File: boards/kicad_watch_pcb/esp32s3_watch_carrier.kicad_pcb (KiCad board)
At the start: 2 copper layers, 180 x 120 mm, 15 parts, among them J1 ESP32-S3 GPIO BUS, J2 ST7735 128x128, J3 I2S MIC, J4 MAX98357A, J5 MPU6050, J6 POWER, SW1 P4, SW2 P5, SW3 P6, SW4 P7

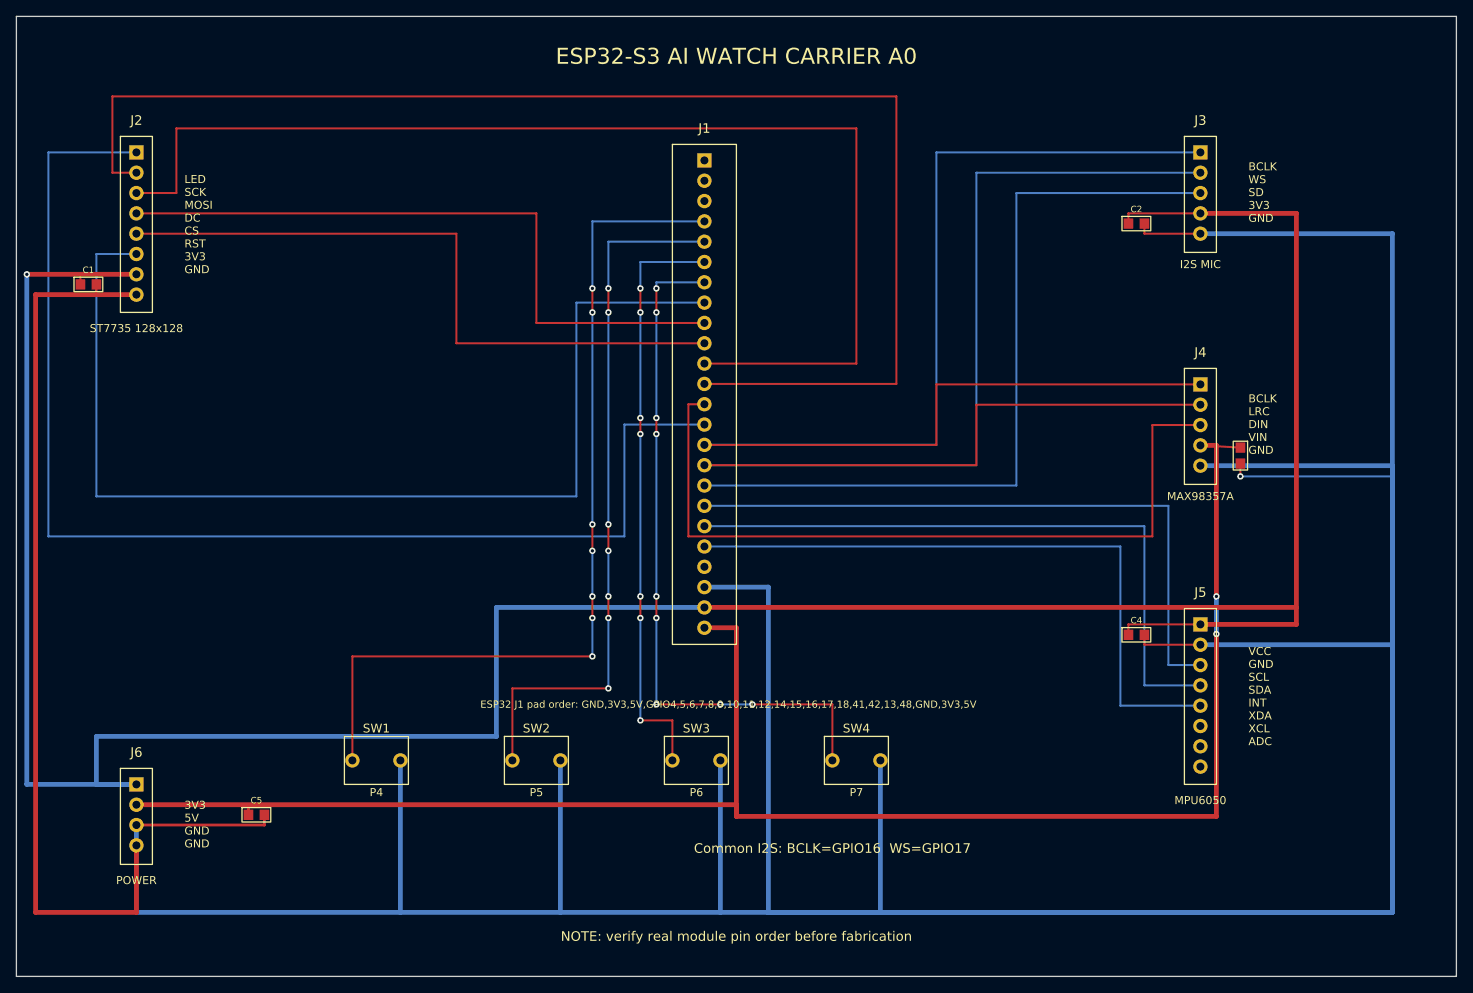
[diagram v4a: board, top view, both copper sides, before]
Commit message: Add ESP32-S3 devkit socket placeholder
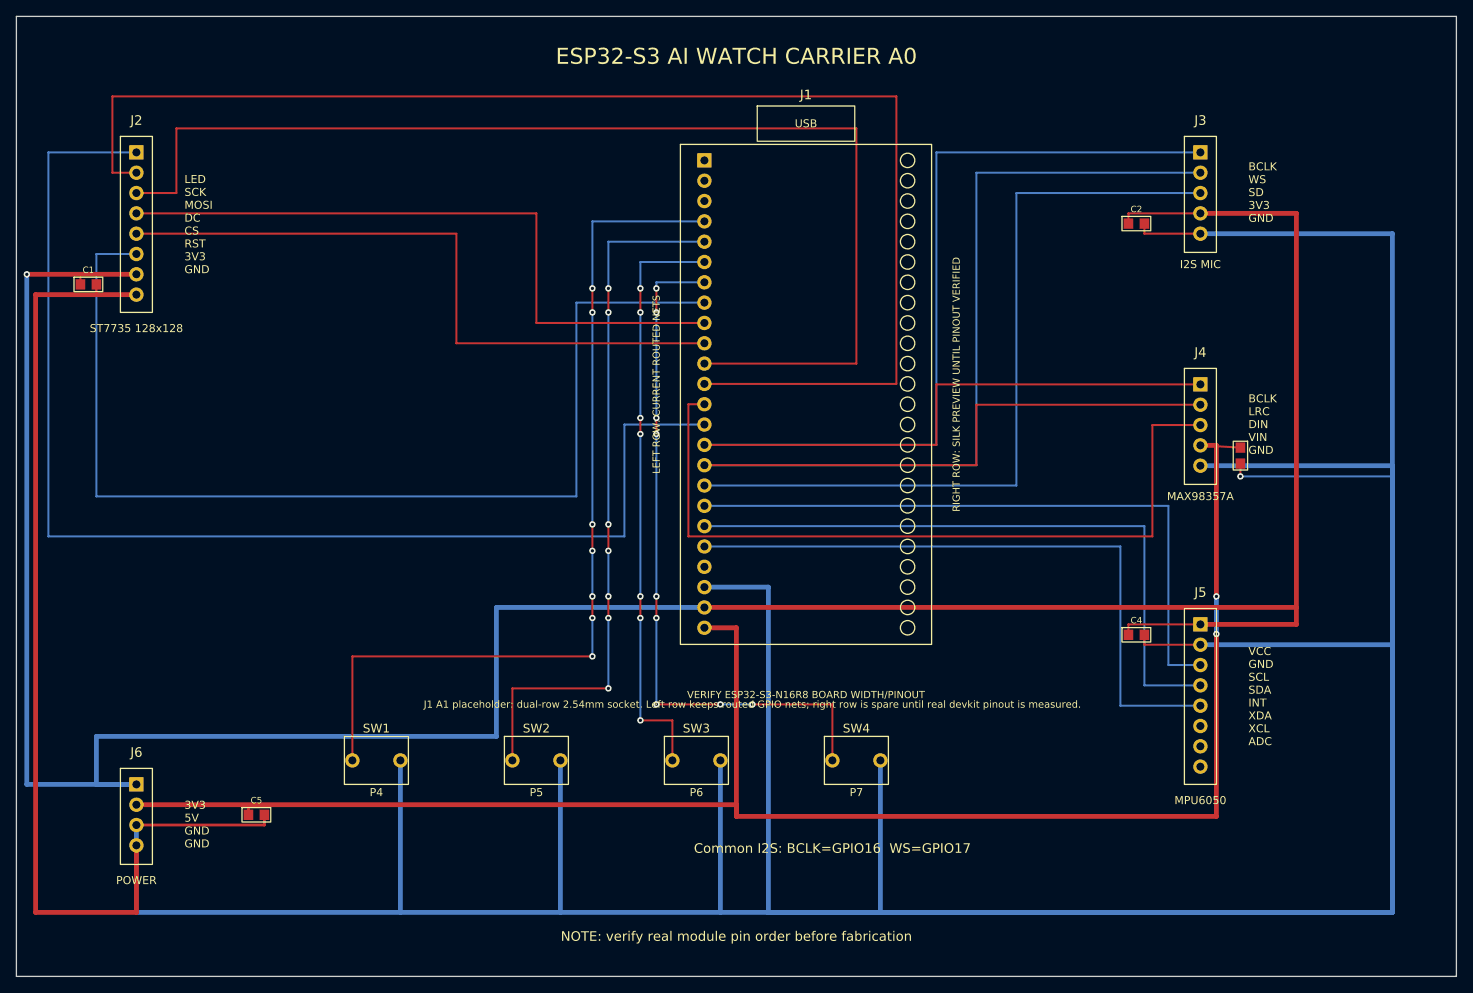
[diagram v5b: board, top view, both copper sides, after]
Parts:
- J1: value ESP32-S3 GPIO BUS -> ESP32-S3 DEVKIT SOCKET A1 PLACEHOLDER; footprint ESP32S3_GPIO_BUS -> ESP32S3_DEVKIT_SOCKET_A1_PLACEHOLDER
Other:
- board text added: "J1 A1 placeholder: dual-row 2.54mm socket. Left row keeps routed GPIO nets; right row is spare until real devkit pinout is measured."
- board text removed: "ESP32 J1 pad order: GND,3V3,5V,GPIO4,5,6,7,8,9,10,11,12,14,15,16,17,18,41,42,13,48,GND,3V3,5V"
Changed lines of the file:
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@@
     (effects (font (size 1.2 1.2) (thickness 0.18)))
   )
-  (footprint "ESP32S3_GPIO_BUS" (layer "F.Cu")
+  (footprint "ESP32S3_DEVKIT_SOCKET_A1_PLACEHOLDER" (layer "F.Cu")
     (at 96 28)
-    (descr "Generic 2.54mm GPIO bus for ESP32-S3 dev board wiring")
-    (tags "ESP32-S3 carrier GPIO bus")
+    (descr "A1 editable 2x24 2.54mm ESP32-S3 dev board socket placeholder; verify exact module pinout before fabrication")
+    (tags "ESP32-S3 devkit socket placeholder verify pinout")
     (attr through_hole)
-    (fp_text reference "J1" (at 0 -4) (layer "F.SilkS")
+    (fp_text reference "J1" (at 12.7 -8.2) (layer "F.SilkS")
       (effects (font (size 1.2 1.2) (thickness 0.18)))
     )
-    (fp_text value "ESP32-S3 GPIO BUS" (at 0 63) (layer "F.Fab")
+    (fp_text value "ESP32-S3 DEVKIT SOCKET A1 PLACEHOLDER" (at 12.7 63) (layer "F.Fab")
       (effects (font (size 1 1) (thickness 0.15)))
     )
-    (fp_rect (start -4 -2) (end 4 60.5) (layer "F.SilkS") (width 0.12))
+    (fp_rect (start -3 -2) (end 28.4 60.5) (layer "F.SilkS") (width 0.12))
+    (fp_rect (start -5 -5) (end 30.4 65) (layer "F.Fab") (width 0.10))
+    (fp_rect (start 6.6 -6.8) (end 18.8 -2.4) (layer "F.SilkS") (width 0.12))
+    (fp_text user "USB" (at 12.7 -4.6) (layer "F.SilkS")
+      (effects (font (size 1 1) (thickness 0.14)))
+    )
+    (fp_text user "LEFT ROW: CURRENT ROUTED NETS" (at -6 28 90) (layer "F.SilkS")
+      (effects (font (size 0.9 0.9) (thickness 0.12)))
+    )
+    (fp_text user "RIGHT ROW: SILK PREVIEW UNTIL PINOUT VERIFIED" (at 31.5 28 90) (layer "F.SilkS")
+      (effects (font (size 0.9 0.9) (thickness 0.12)))
+    )
+    (fp_text user "VERIFY ESP32-S3-N16R8 BOARD WIDTH/PINOUT" (at 12.7 66.8) (layer "F.SilkS")
+      (effects (font (size 0.9 0.9) (thickness 0.12)))
+    )
     (pad "1" thru_hole rect (at 0 0) (size 1.8 1.8) (drill 1) (layers *.Cu *.Mask))
     (pad "2" thru_hole oval (at 0 2.54) (size 1.8 1.8) (drill 1) (layers *.Cu *.Mask))
@@
     (pad "23" thru_hole oval (at 0 55.88) (size 1.8 1.8) (drill 1) (layers *.Cu *.Mask) (net 2 "3V3"))
     (pad "24" thru_hole oval (at 0 58.42) (size 1.8 1.8) (drill 1) (layers *.Cu *.Mask) (net 3 "5V"))
+    (fp_circle (center 25.4 0) (end 26.30 0) (layer "F.SilkS") (width 0.10))
+    (fp_circle (center 25.4 2.54) (end 26.30 2.54) (layer "F.SilkS") (width 0.10))
+    (fp_circle (center 25.4 5.08) (end 26.30 5.08) (layer "F.SilkS") (width 0.10))
+    (fp_circle (center 25.4 7.62) (end 26.30 7.62) (layer "F.SilkS") (width 0.10))
+    (fp_circle (center 25.4 10.16) (end 26.30 10.16) (layer "F.SilkS") (width 0.10))
+    (fp_circle (center 25.4 12.7) (end 26.30 12.7) (layer "F.SilkS") (width 0.10))
+    (fp_circle (center 25.4 15.24) (end 26.30 15.24) (layer "F.SilkS") (width 0.10))
+    (fp_circle (center 25.4 17.78) (end 26.30 17.78) (layer "F.SilkS") (width 0.10))
+    (fp_circle (center 25.4 20.32) (end 26.30 20.32) (layer "F.SilkS") (width 0.10))
+    (fp_circle (center 25.4 22.86) (end 26.30 22.86) (layer "F.SilkS") (width 0.10))
+    (fp_circle (center 25.4 25.4) (end 26.30 25.4) (layer "F.SilkS") (width 0.10))
+    (fp_circle (center 25.4 27.94) (end 26.30 27.94) (layer "F.SilkS") (width 0.10))
+    (fp_circle (center 25.4 30.48) (end 26.30 30.48) (layer "F.SilkS") (width 0.10))
+    (fp_circle (center 25.4 33.02) (end 26.30 33.02) (layer "F.SilkS") (width 0.10))
+    (fp_circle (center 25.4 35.56) (end 26.30 35.56) (layer "F.SilkS") (width 0.10))
+    (fp_circle (center 25.4 38.1) (end 26.30 38.1) (layer "F.SilkS") (width 0.10))
+    (fp_circle (center 25.4 40.64) (end 26.30 40.64) (layer "F.SilkS") (width 0.10))
+    (fp_circle (center 25.4 43.18) (end 26.30 43.18) (layer "F.SilkS") (width 0.10))
+    (fp_circle (center 25.4 45.72) (end 26.30 45.72) (layer "F.SilkS") (width 0.10))
+    (fp_circle (center 25.4 48.26) (end 26.30 48.26) (layer "F.SilkS") (width 0.10))
+    (fp_circle (center 25.4 50.8) (end 26.30 50.8) (layer "F.SilkS") (width 0.10))
+    (fp_circle (center 25.4 53.34) (end 26.30 53.34) (layer "F.SilkS") (width 0.10))
+    (fp_circle (center 25.4 55.88) (end 26.30 55.88) (layer "F.SilkS") (width 0.10))
+    (fp_circle (center 25.4 58.42) (end 26.30 58.42) (layer "F.SilkS") (width 0.10))
   )
   (footprint "TFT_ST7735_HEADER" (layer "F.Cu")
@@
     (pad "2" thru_hole circle (at 3 0) (size 1.8 1.8) (drill 1) (layers *.Cu *.Mask) (net 1 "GND"))
   )
-  (gr_text "ESP32 J1 pad order: GND,3V3,5V,GPIO4,5,6,7,8,9,10,11,12,14,15,16,17,18,41,42,13,48,GND,3V3,5V" (at 99 96) (layer "F.SilkS")
+  (gr_text "J1 A1 placeholder: dual-row 2.54mm socket. Left row keeps routed GPIO nets; right row is spare until real devkit pinout is measured." (at 102 96) (layer "F.SilkS")
     (effects (font (size 0.9 0.9) (thickness 0.12)))
   )
